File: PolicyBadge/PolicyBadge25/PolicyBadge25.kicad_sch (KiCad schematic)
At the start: 10 parts, among them CN1 PH2.0-2P-LT, J1 Feed Point 915MHz, J4 Feed Point 2.4 GHz, SW3 TA-3525-A1, U1 MOUDLE-SEEEDUINO-XIAO-ESP32S3

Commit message: IO sheet
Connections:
- net INT_N: now reaches U1.2 (PA4_A1_D1)
- net Buzzer: now reaches U1.4 (PA11_A3_D3)
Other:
- added sheet IO (io.kicad_sch)

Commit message: Released version of PCB
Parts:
- added H1: MH254V-11-04-1000, imported:HDR-TH_4P-P2.54-V-M-3, symbol JLCPCB:MH254V-11-04-1000
- added U1: HS96L03W2C03, imported:OLED-TH_L27.8-W27.2-P2.54_C9900033791, symbol JLCPCB:HS96L03W2C03
- U2: renamed from U1; footprint MOUDLE14P-SMD-2.54-21X17.8MM -> XAIO ESP32S3:MOUDLE14P-SMD-2.54-21X17.8MM-header
- renumbered J4 to J2, R7 to R3, R6 to R4, SW3 to SW1
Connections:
- net GND: now also H1.1, U1.1 (GND)
- net SDA: now also H1.4, U1.4 (SDA)
- net VBATT+: now also SW1.3 (C); no longer SW1.1 (A)
- net VCC_3V3: now also U2.12 (3V3), H1.2, U1.2 (VCC)
- net IO Expander and LED's/IO_INT: now reaches U2.1 (PA02_A0_D0)
- net Buzzer: no longer names the net of U2.4 (PA11_A3_D3)
- net INT_N renamed IO Expander and LED's/BUZZER
- net SDC renamed SCL
- net SCL: now also H1.3, U1.3 (SCL)
- no-connect marks 0 -> 14
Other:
- removed sheet IO
- added sheet IO Expander and LED's (ioexpander.kicad_sch)
- note added: "Screen and pin header"
- moved on the sheet: CN1, J1, J2, R1, R2, R3, R4, SW1, U2, USB1

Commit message: Added batt monitoring
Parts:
- added R5, R6: 220kΩ, imported:R0603, symbol JLCPCB:0603WAF2203T5E
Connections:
- net GND: now also R6.1
- net IO Expander and LED's/BUZZER: now also U2.3 (PA10_A2_D2); no longer U2.2 (PA4_A1_D1)
- net IO Expander and LED's/IO_INT: now also U2.2 (PA4_A1_D1); no longer U2.1 (PA02_A0_D0)
- net VBATT+: now also R5.2
- new net: R5.1, R6.2, U2.1 (PA02_A0_D0)
- no-connect marks 14 -> 13

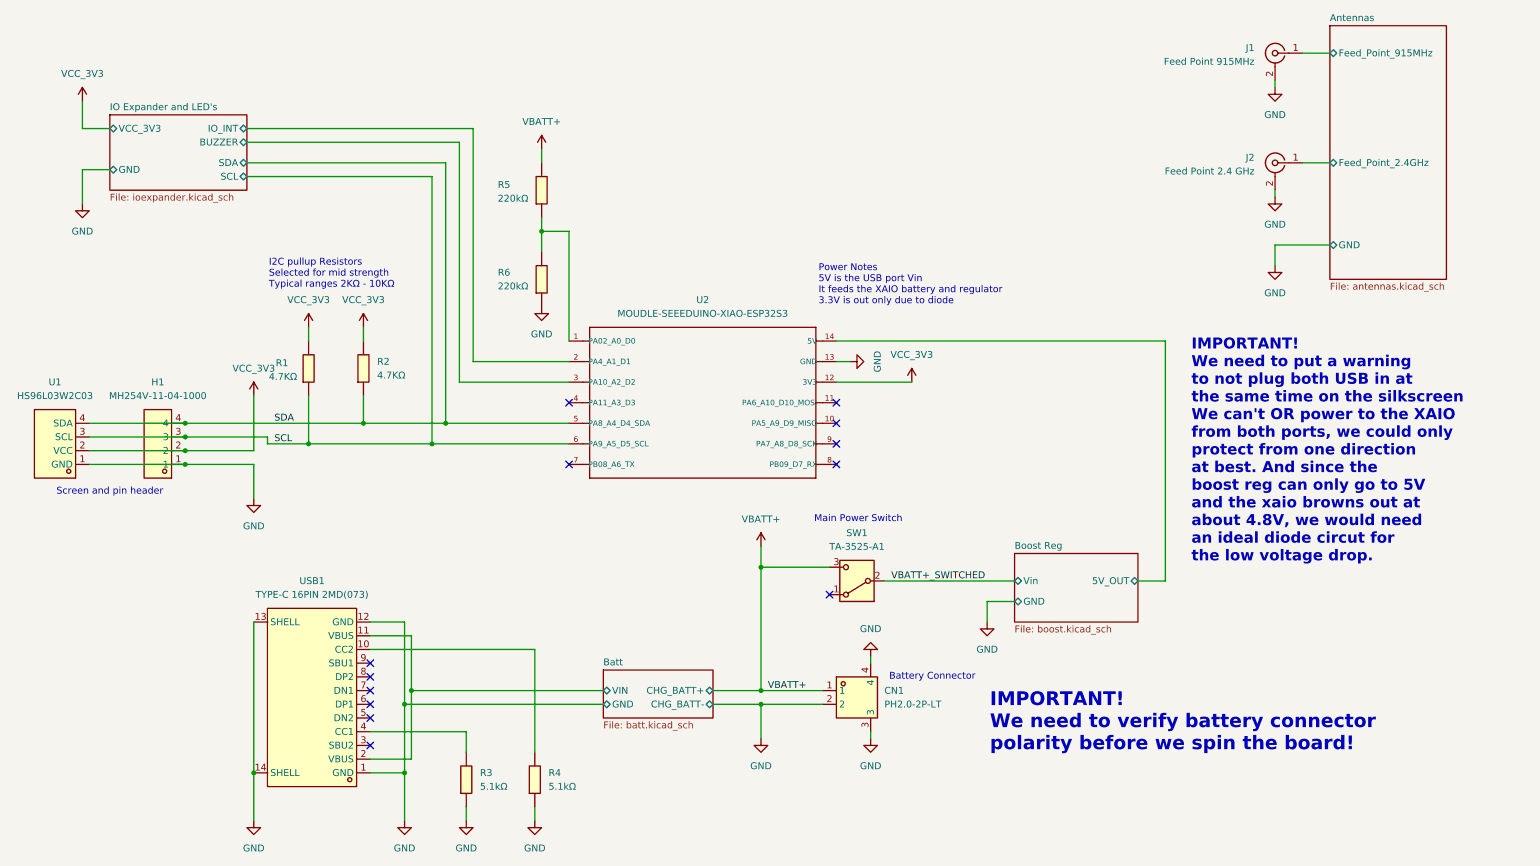
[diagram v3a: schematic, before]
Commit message: Lots of changes, laying out board for board shape
Updated switches
Added headers for XAIO
Fixed Batt Connector polarity
10K pullup on int
Batt monitor resistor divider
Fix buzzer trace
XAIO footprint spacing
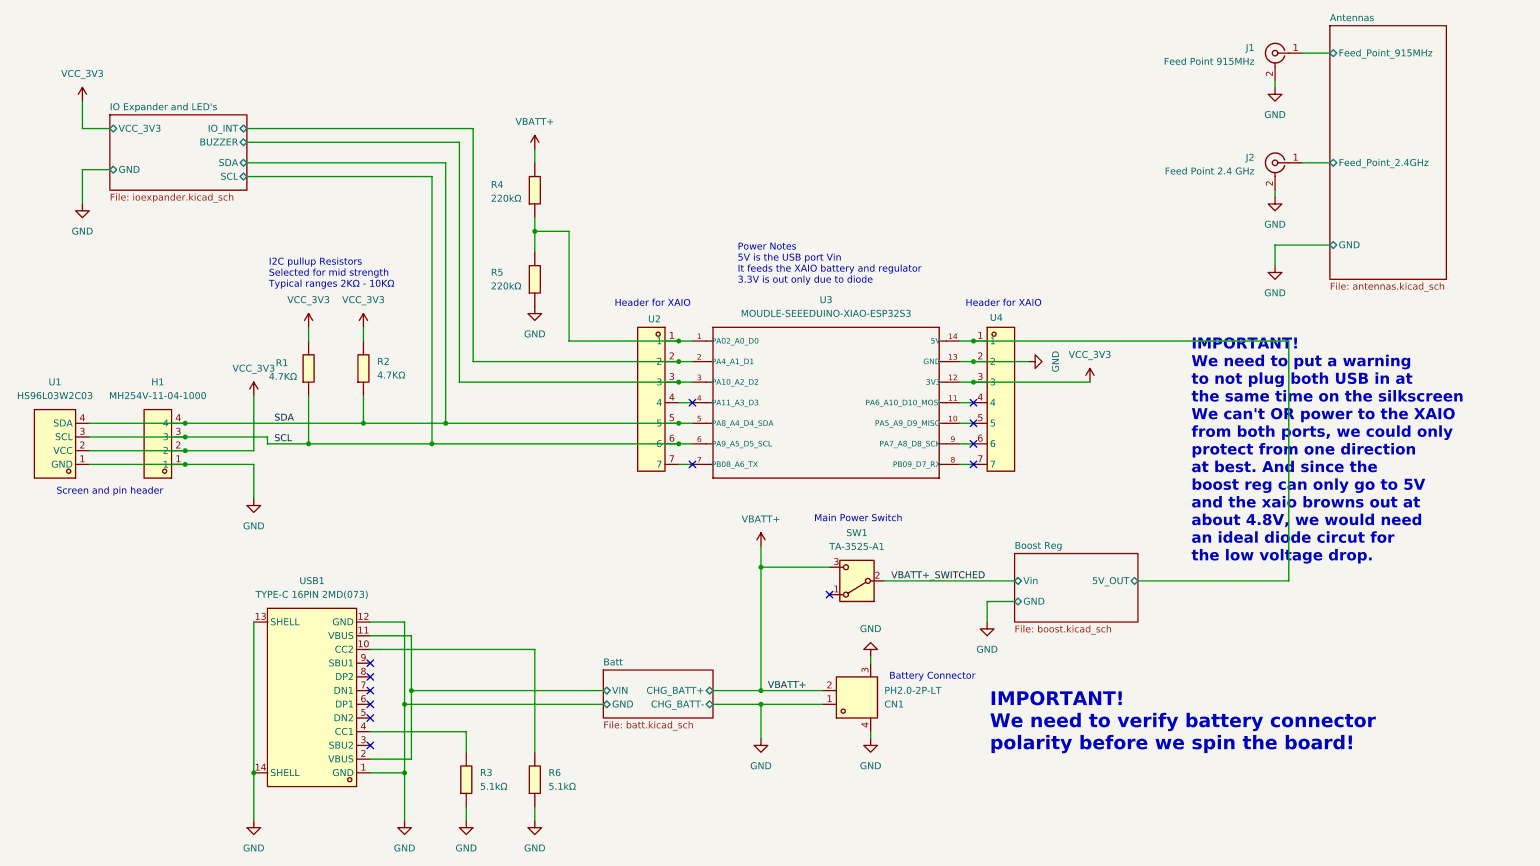
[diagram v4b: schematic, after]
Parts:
- added U2, U4: ~, imported:HDR-TH_7P-P2.54-V-F, symbol JLCPCB:DM254R-11-07-85
- U3: renamed from U2; footprint XAIO ESP32S3:MOUDLE14P-SMD-2.54-21X17.8MM-header -> XAIO ESP32S3:MOUDLE14P-SMD-2.54-21X17.8MM-header-fixed
- renumbered R5 to R4, R6 to R5, R4 to R6
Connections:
- net Boost Reg/5V_OUT: now also U4.1
- net GND: now also CN1.1, U4.2; no longer CN1.2
- net IO Expander and LED's/BUZZER: now also U2.3
- net IO Expander and LED's/IO_INT: now also U2.2
- net SCL: now also U2.6
- net SDA: now also U2.5
- net VBATT+: now also CN1.2; no longer CN1.1
- net VCC_3V3: now also U4.3
- net at R4.1, R5.2, U3.1 (PA02_A0_D0): now also U2.1
- net at U3.10 (PA5_A9_D9_MISO): now also U4.5
- net at U3.11 (PA6_A10_D10_MOSI): now also U4.4
- net at U3.4 (PA11_A3_D3): now also U2.4
- net at U3.7 (PB08_A6_TX): now also U2.7
- net at U3.8 (PB09_D7_RX): now also U4.7
- net at U3.9 (PA7_A8_D8_SCK): now also U4.6
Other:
- note added: "Header for XAIO"
- moved on the sheet: R4, R5, U3
